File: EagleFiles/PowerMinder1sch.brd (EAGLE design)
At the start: 25.1 x 62.2 mm, 14 parts

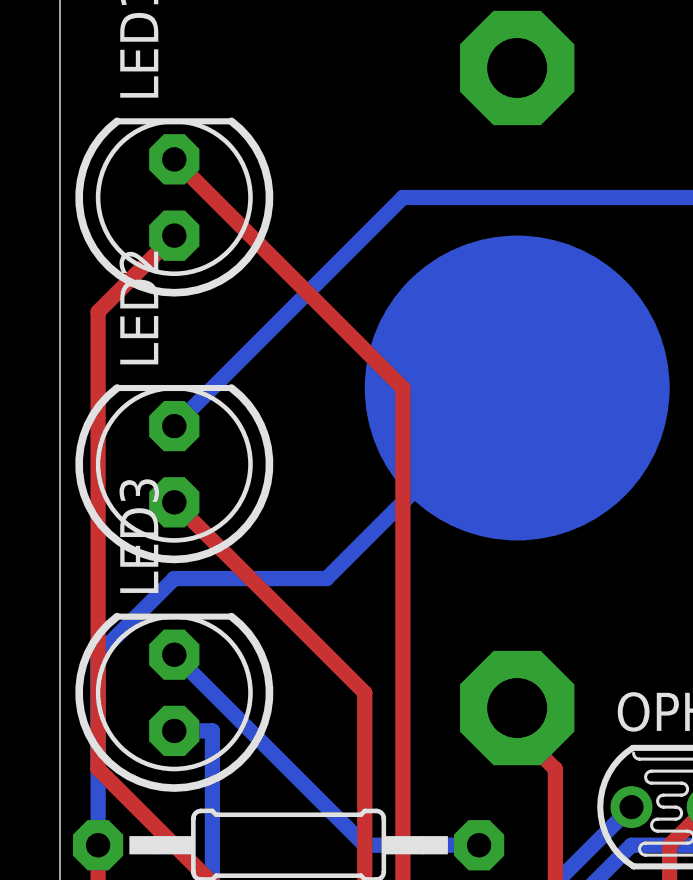
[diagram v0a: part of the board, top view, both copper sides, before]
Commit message: DigiSparkArduino now compiles the code.
No Calendar.cpp code incorporated into main program yet.  Concentrated
on compilation.

For Eagle files made micro adjustments to component positions.  Do not
yet trust the Eagle files as they are untested and unverified.  Three
prototype are being built to verify the design.
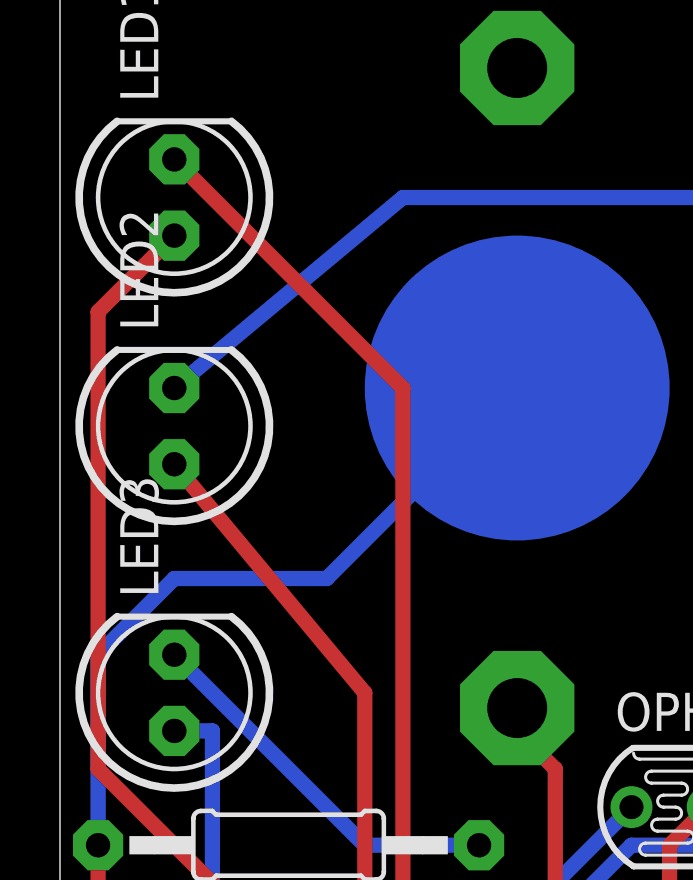
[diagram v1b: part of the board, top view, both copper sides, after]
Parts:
- moved LED2 1.27 mm to (3.81, 47.0)
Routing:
- net N$2: track 44.4 -> 45.4 mm
- net N$6: track 57.3 -> 56.5 mm
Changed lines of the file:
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@@
 <element name="CR2032" library="adafruit" package="CR2032-THRU" value="3V" x="15.24" y="48.26" rot="MR90"/>
 <element name="LED1" library="adafruit" package="LED5MM" value="RED" x="3.81" y="54.61" rot="R90"/>
-<element name="LED2" library="adafruit" package="LED5MM" value="AMBER" x="3.81" y="45.72" rot="R90"/>
+<element name="LED2" library="adafruit" package="LED5MM" value="AMBER" x="3.81" y="46.99" rot="R90"/>
 <element name="LED3" library="adafruit" package="LED5MM" value="GREEN" x="3.81" y="38.1" rot="R90"/>
 <element name="R1" library="adafruit" package="0207/12" value="150" x="7.62" y="21.59" rot="R180"/>
@@
 <wire x1="13.97" y1="8.89" x2="13.97" y2="16.51" width="0.508" layer="1"/>
 <wire x1="16.51" y1="6.35" x2="13.97" y2="8.89" width="0.508" layer="1"/>
-<wire x1="10.16" y1="38.1" x2="3.81" y2="44.45" width="0.508" layer="1"/>
+<wire x1="10.16" y1="38.1" x2="3.81" y2="45.72" width="0.508" layer="1"/>
 <wire x1="10.16" y1="22.86" x2="10.16" y2="38.1" width="0.508" layer="1"/>
 <wire x1="15.24" y1="17.78" x2="10.16" y2="22.86" width="0.508" layer="1"/>
@@
 <wire x1="22.86" y1="54.61" x2="22.86" y2="33.02" width="0.508" layer="16"/>
 <wire x1="11.43" y1="54.61" x2="22.86" y2="54.61" width="0.508" layer="16"/>
-<wire x1="3.81" y1="46.99" x2="11.43" y2="54.61" width="0.508" layer="16"/>
+<wire x1="3.81" y1="48.26" x2="11.43" y2="54.61" width="0.508" layer="16"/>
 </signal>
 <signal name="N$7">

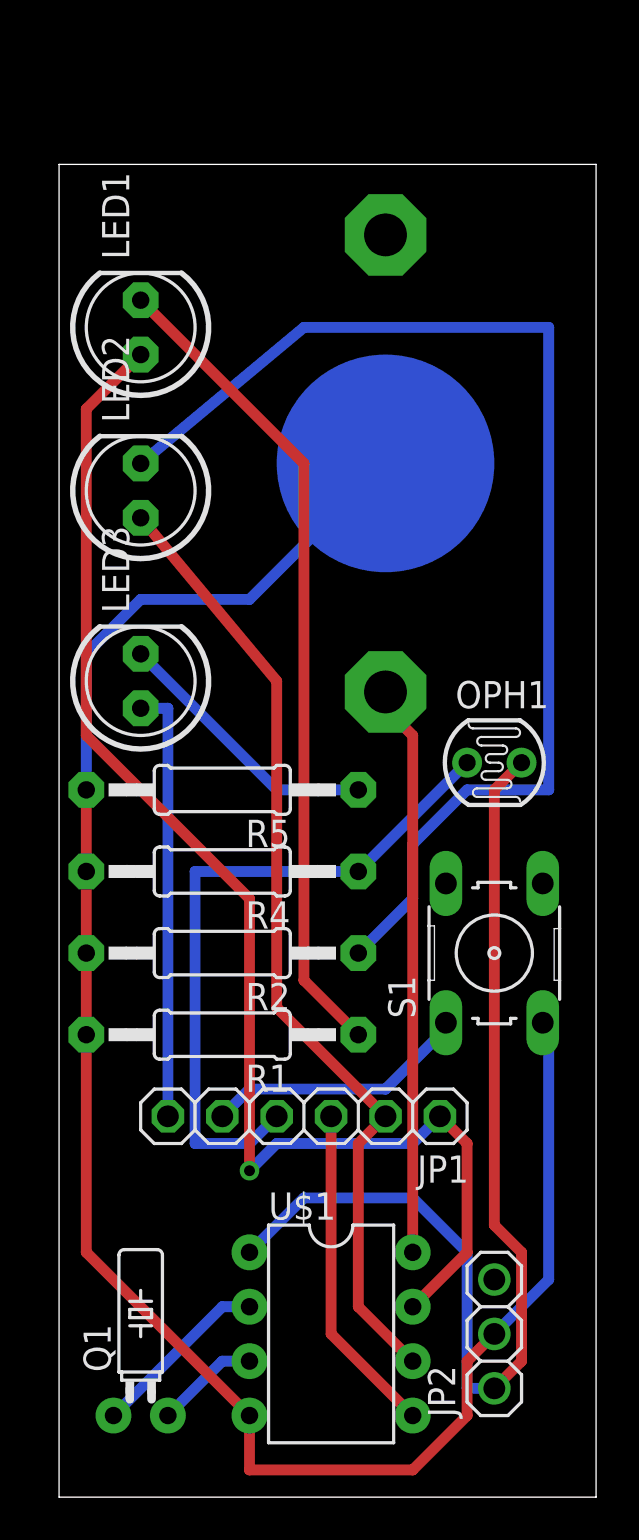
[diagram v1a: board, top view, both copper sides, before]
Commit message: Fixed board
Proto BRD now probably functional.  Original button now goes high and
added a resistor to GND.  Value for R are all TBD.  Battery holder will
need to be moved as it may hit the LED pins.
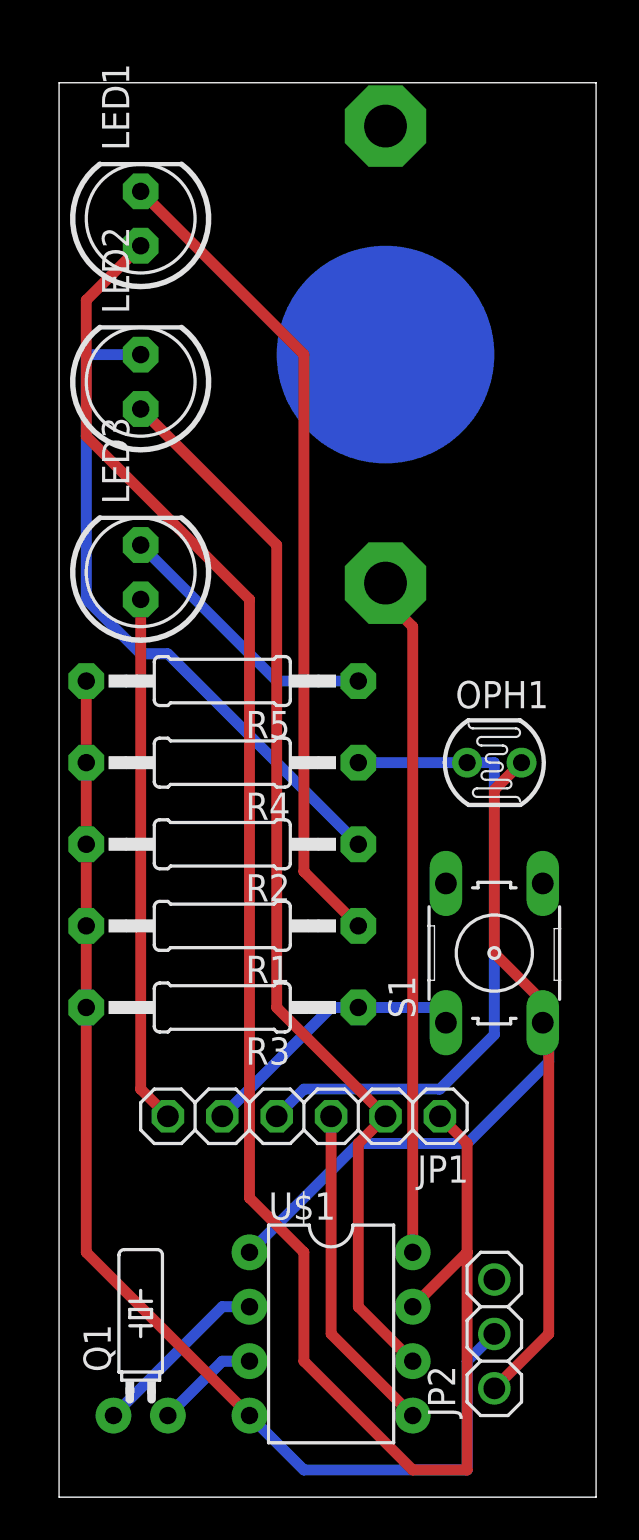
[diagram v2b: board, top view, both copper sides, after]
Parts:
- added R3: 82, adafruit:0207/12
- moved CR2032 5.08 mm to (15.2, 53.3)
- moved R1 5.08 mm to (7.62, 26.7)
- moved R2 5.08 mm to (7.62, 30.5)
- moved LED1 5.08 mm to (3.81, 59.7)
- moved LED2 5.08 mm to (3.81, 52.1)
- moved LED3 5.08 mm to (3.81, 43.2)
- moved R4 5.08 mm to (7.62, 34.3)
- moved R5 5.08 mm to (7.62, 38.1)
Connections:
- net +5V: now also S1.3
- net GND: now also R3.2; no longer S1.3
- net N$11: now also R3.1
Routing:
- net GND: track 90.1 -> 55.5 mm
- net N$6: track 56.5 -> 31.4 mm
- net N$1: track 62.7 -> 87.7 mm, vias 1 -> 0
- net N$2: track 45.4 -> 50.8 mm
- net N$10: track 26.7 -> 31.8 mm
- net N$4: track 20.3 -> 24.7 mm
- net N$3: track 31.8 -> 30.8 mm
- net +5V: track 50.7 -> 51.5 mm
- net N$11: track 12.4 -> 13.0 mm
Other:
- board size 25.1 x 62.2 mm -> 25.1 x 66 mm

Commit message: Proto board V2
Layout changes - may help with battery position.  Resistors moved to
help with routing - needs more work - suits the prototype need for now.
 Expect Proto v4 to be the board  that is stable enough for the project
to make you own.
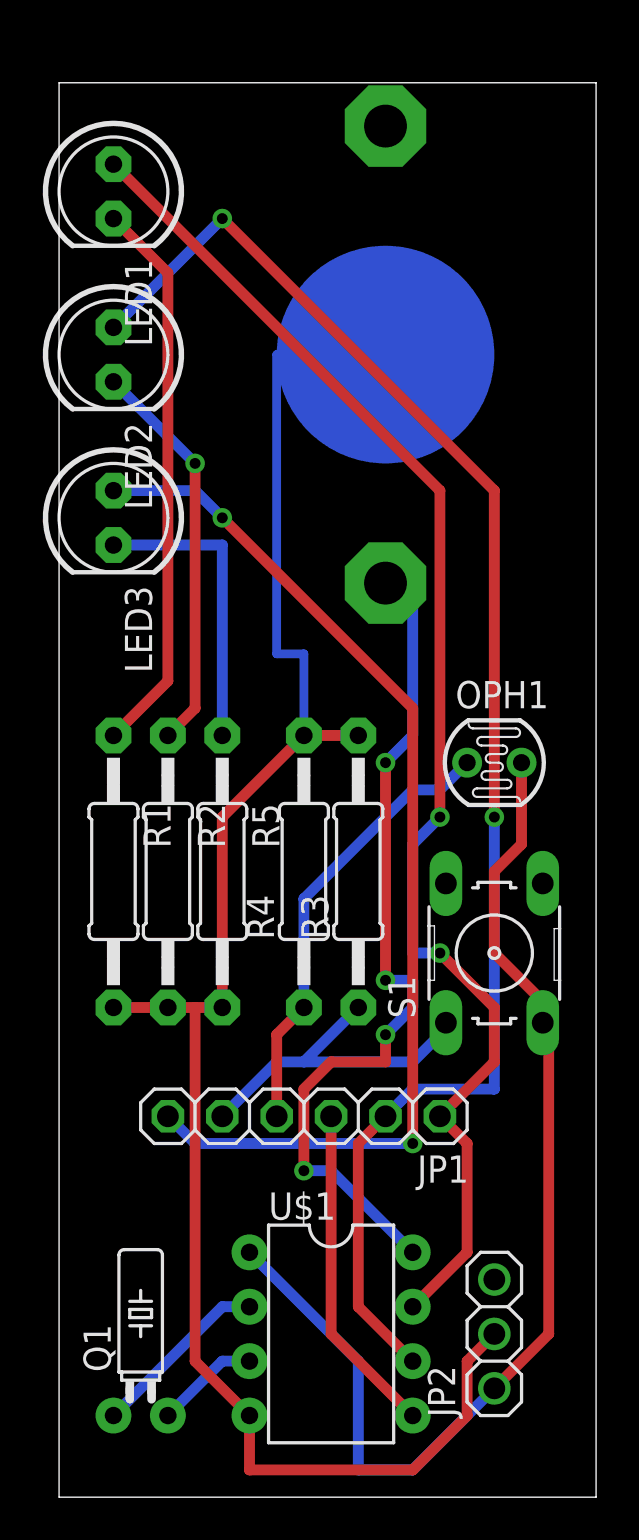
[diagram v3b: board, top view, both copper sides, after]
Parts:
- moved R3 8.98 mm to (14.0, 29.2), turned to 90 degrees
- moved R5 8.89 mm to (7.62, 29.2), turned to 270 degrees
- moved R4 6.35 mm to (11.4, 29.2), turned to 90 degrees
- moved R1 5.68 mm to (2.54, 29.2), turned to 270 degrees
- moved R2 2.84 mm to (5.08, 29.2), turned to 270 degrees
- moved LED3 2.84 mm to (2.54, 45.7), turned to 270 degrees
- moved LED1 1.80 mm to (2.54, 61.0), turned to 270 degrees
- moved LED2 1.80 mm to (2.54, 53.3), turned to 270 degrees
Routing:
- net GND: track 55.5 -> 84.2 mm
- net N$4: track 24.7 -> 50.5 mm, vias 0 -> 2
- net N$1: track 87.7 -> 65.1 mm, vias 0 -> 2
- net N$2: track 50.8 -> 71.7 mm, vias 0 -> 2
- net N$6: track 31.4 -> 18.6 mm, vias 0 -> 1
- net N$5: track 38.5 -> 26.2 mm
- net N$3: track 30.8 -> 20.9 mm
- net N$10: track 31.8 -> 40.7 mm, vias 0 -> 4
- net N$11: track 13.0 -> 16.0 mm
- net N$7: track 12.8 -> 14.0 mm
- net +5V: track 51.5 -> 52.2 mm
